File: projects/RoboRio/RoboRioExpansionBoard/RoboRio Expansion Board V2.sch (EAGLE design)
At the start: 89 parts, among them J1 RRINTERFACE-FEMALE, J2 MICROSD, Q1 5.0 MHz, T1 NPN-SOT416, U1 P8X32A-Q44, U2 24LC256ST, U3 FT232RFTR232R, U4 MC1525TO, U6 RT9193-33GB, U7 RT9193-33GB

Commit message: More updates to power supply
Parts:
- added D4: SSA34-E3/61T, diode:DIODE-DO-214AC
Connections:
- new net N$24: D4.A, J1.P1-5V, U$1.V+, U$10.V+, U$11.V+, U$12.V+, U$2.V+, U$5.V+, U$6.V+, U$7.V+, U$8.V+, U$9.V+
- new net N$25: U6.EN
- net +5V: now also D4.C; no longer U$1.V+, U$10.V+, U$11.V+, U$12.V+, U$2.V+, U$5.V+, U$6.V+, U$7.V+, U$8.V+, U$9.V+, U6.EN
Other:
- note added: "Invert then connect to CBUS 2"
- moved on the sheet: C10, C11, C12, C13, U6

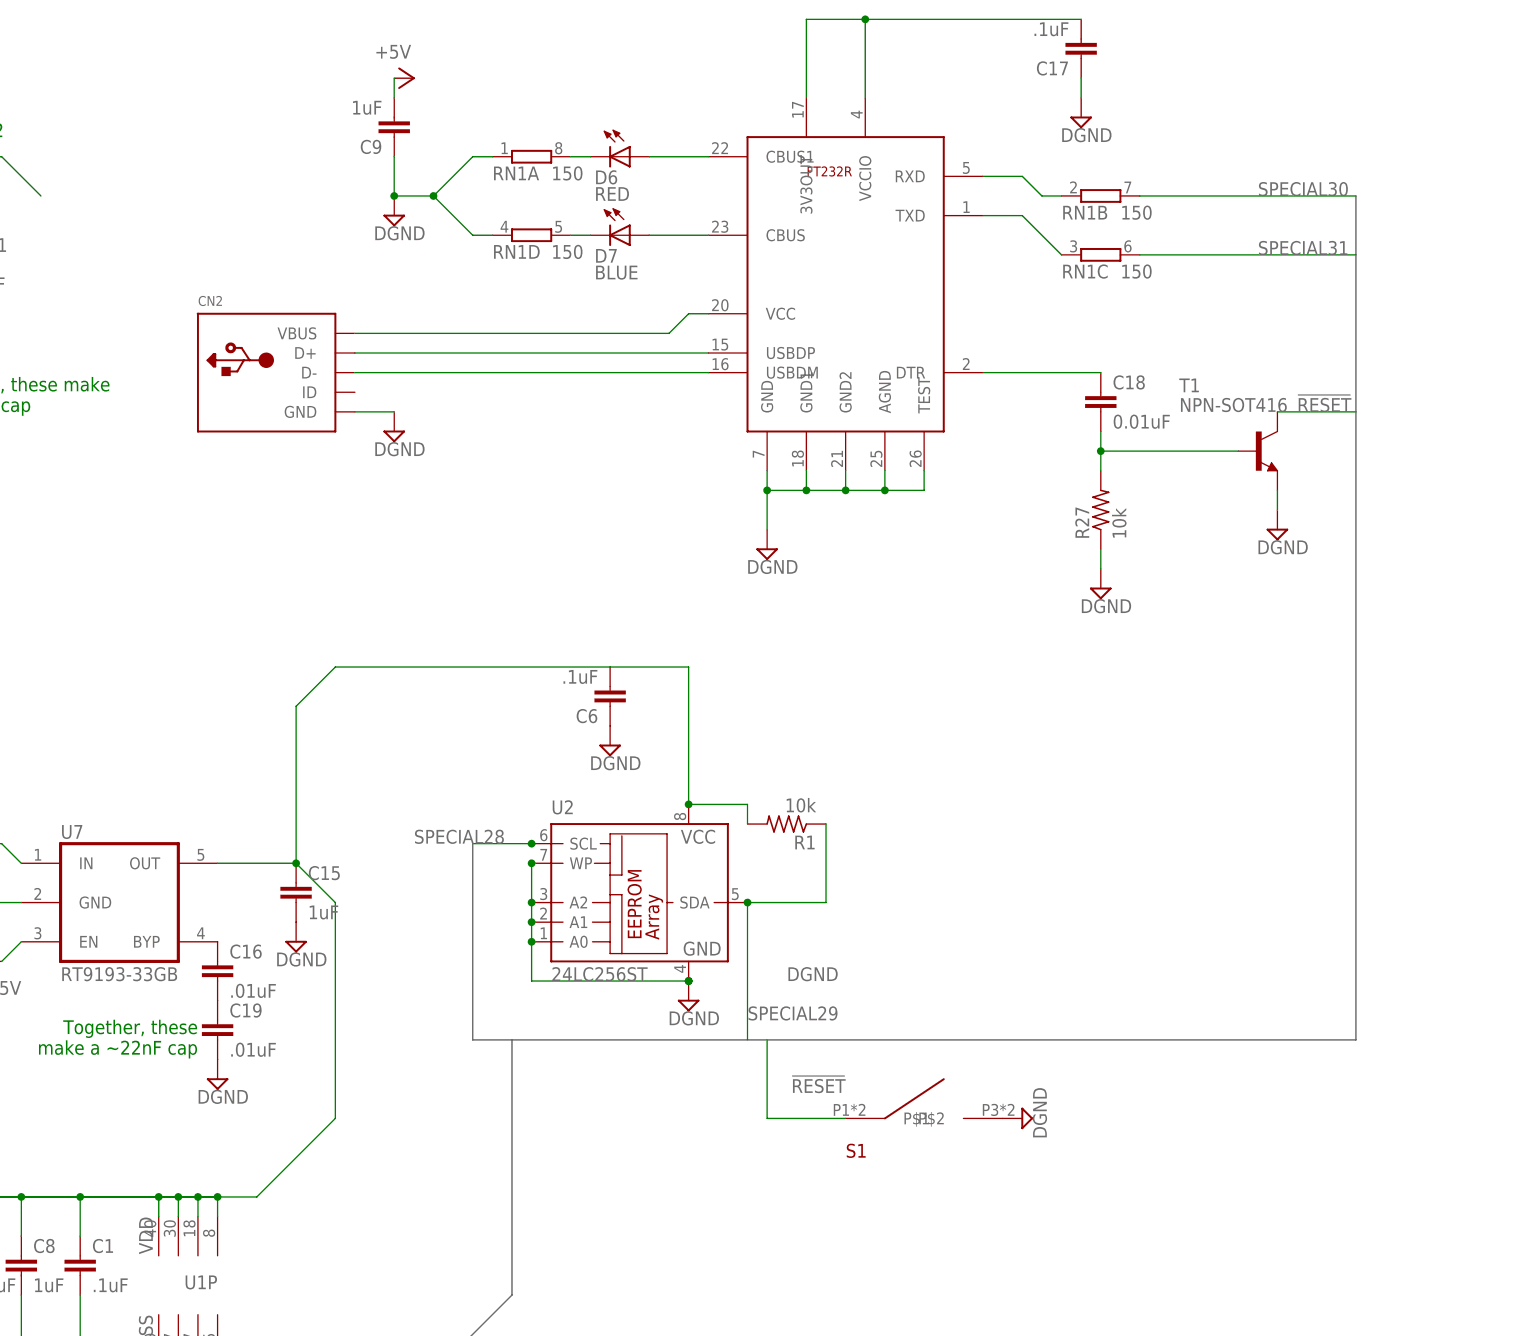
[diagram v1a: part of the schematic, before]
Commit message: Realized that we already had a full FT232R library
Switched over, prepped for the 3v3 reg, though that still needs some
help.
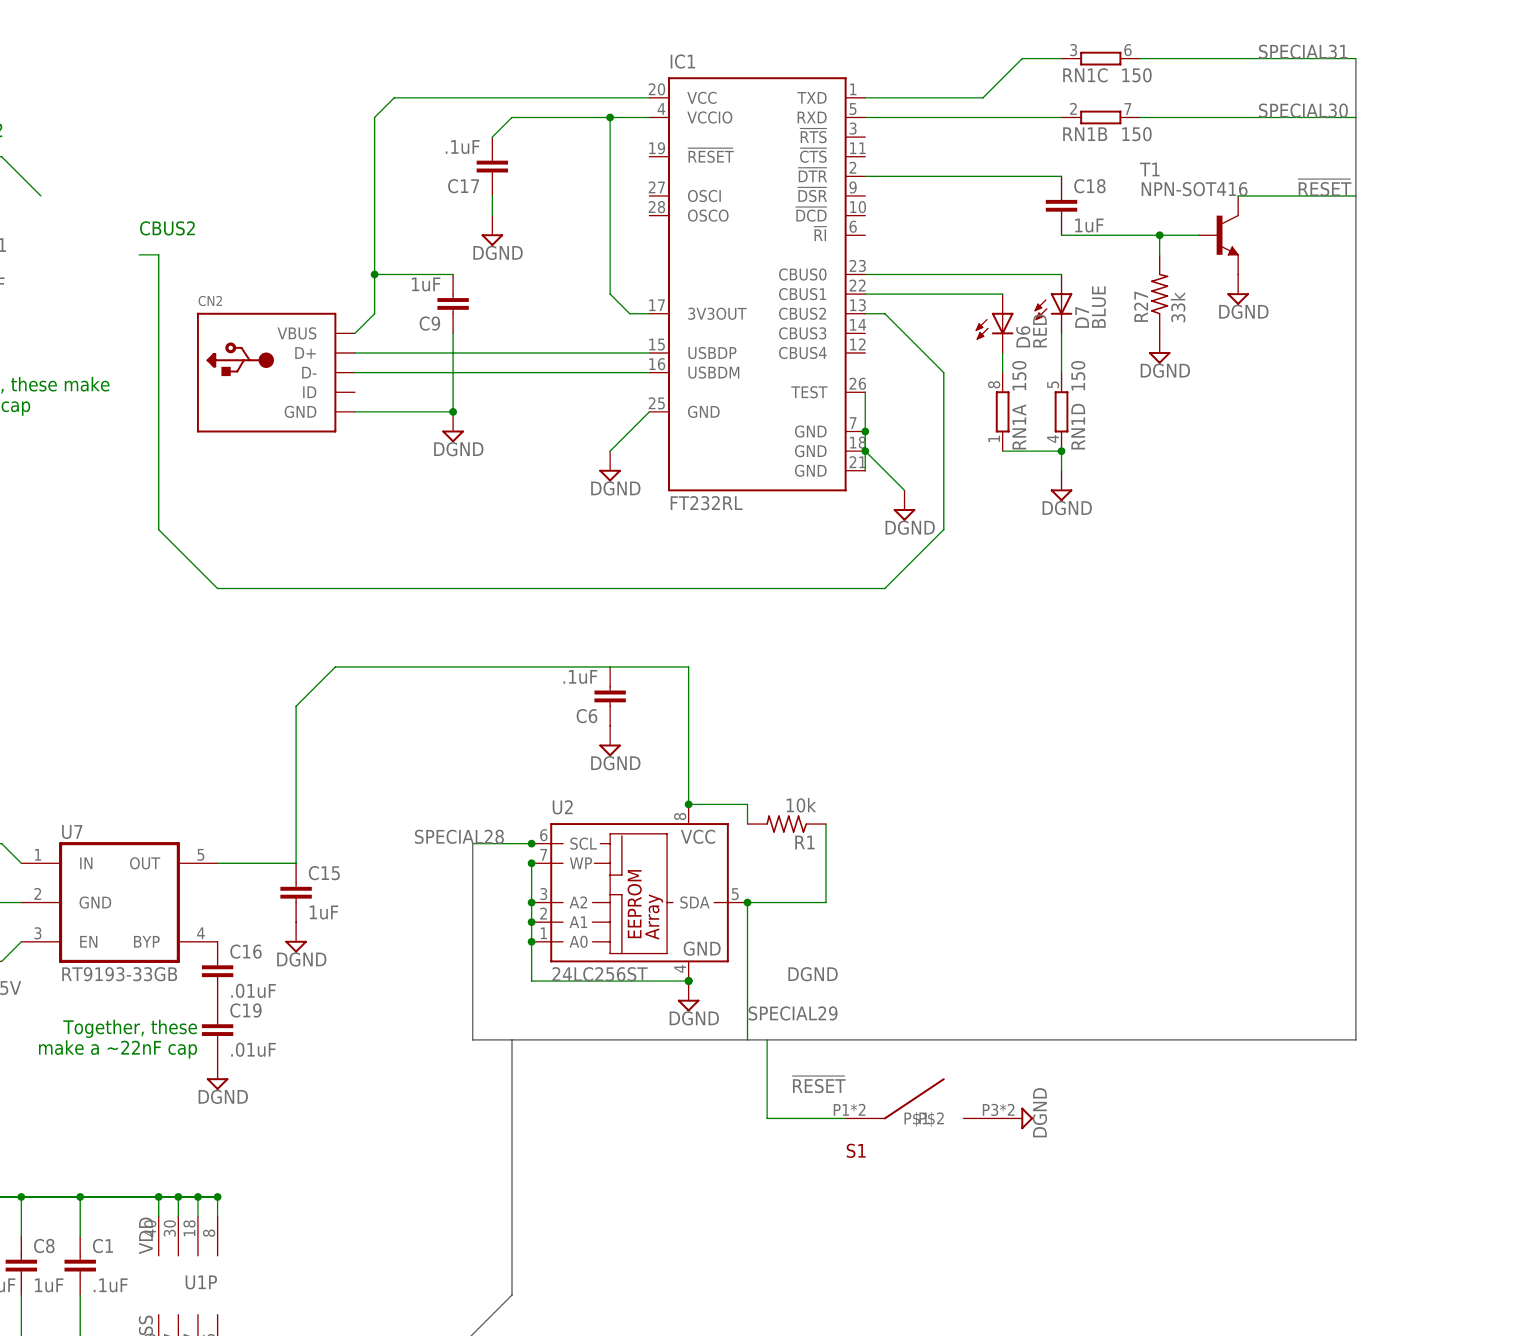
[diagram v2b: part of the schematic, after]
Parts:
- removed U3: FT232RFTR232R, FT232R:FT232RFTR232R
- added IC1: FT232RL, ftdichip:FT232RL
- C18: value 0.01uF -> 1uF
- R27: value 10k -> 33k
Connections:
- removed net N$RX: D6.A, U3.CBUS1
- removed net N$TX: D7.A, U3.CBUS
- new net N$21: C1.1, C7.1, C8.1, U1P.VDD@1, U1P.VDD@2, U1P.VDD@3, U1P.VDD@4
- new net N$27: D7.A, IC1.CBUS0
- new net N$28: D6.A, IC1.CBUS1
- new net N$31: IC1.CBUS2
- net +3V3_PROP: no longer C1.1, C7.1, C8.1, U1P.VDD@1, U1P.VDD@2, U1P.VDD@3, U1P.VDD@4
- net +5V: no longer C9.2
- net DGND: now also IC1.GND, IC1.GND@1, IC1.GND@2, IC1.GND@A, IC1.TEST; no longer U3.AGND, U3.GND, U3.GND1, U3.GND2, U3.TEST
- net N$1: now also IC1.USBDP; no longer U3.USBDP
- net N$19: now also IC1.!DTR; no longer U3.DTR
- net N$2: now also IC1.USBDM; no longer U3.USBDM
- net N$23: now also IC1.TXD; no longer U3.TXD
- net N$3: now also IC1.3V3OUT, IC1.VCCIO; no longer U3.3V3OUT, U3.VCCIO
- net N$5: now also C9.2, IC1.VCC; no longer U3.VCC
- net N$6: now also IC1.RXD; no longer U3.RXD
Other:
- note added: "CBUS2"
- moved on the sheet: C17, C18, C9, D6, D7, R27, RN1A, RN1B, RN1C, RN1D, T1

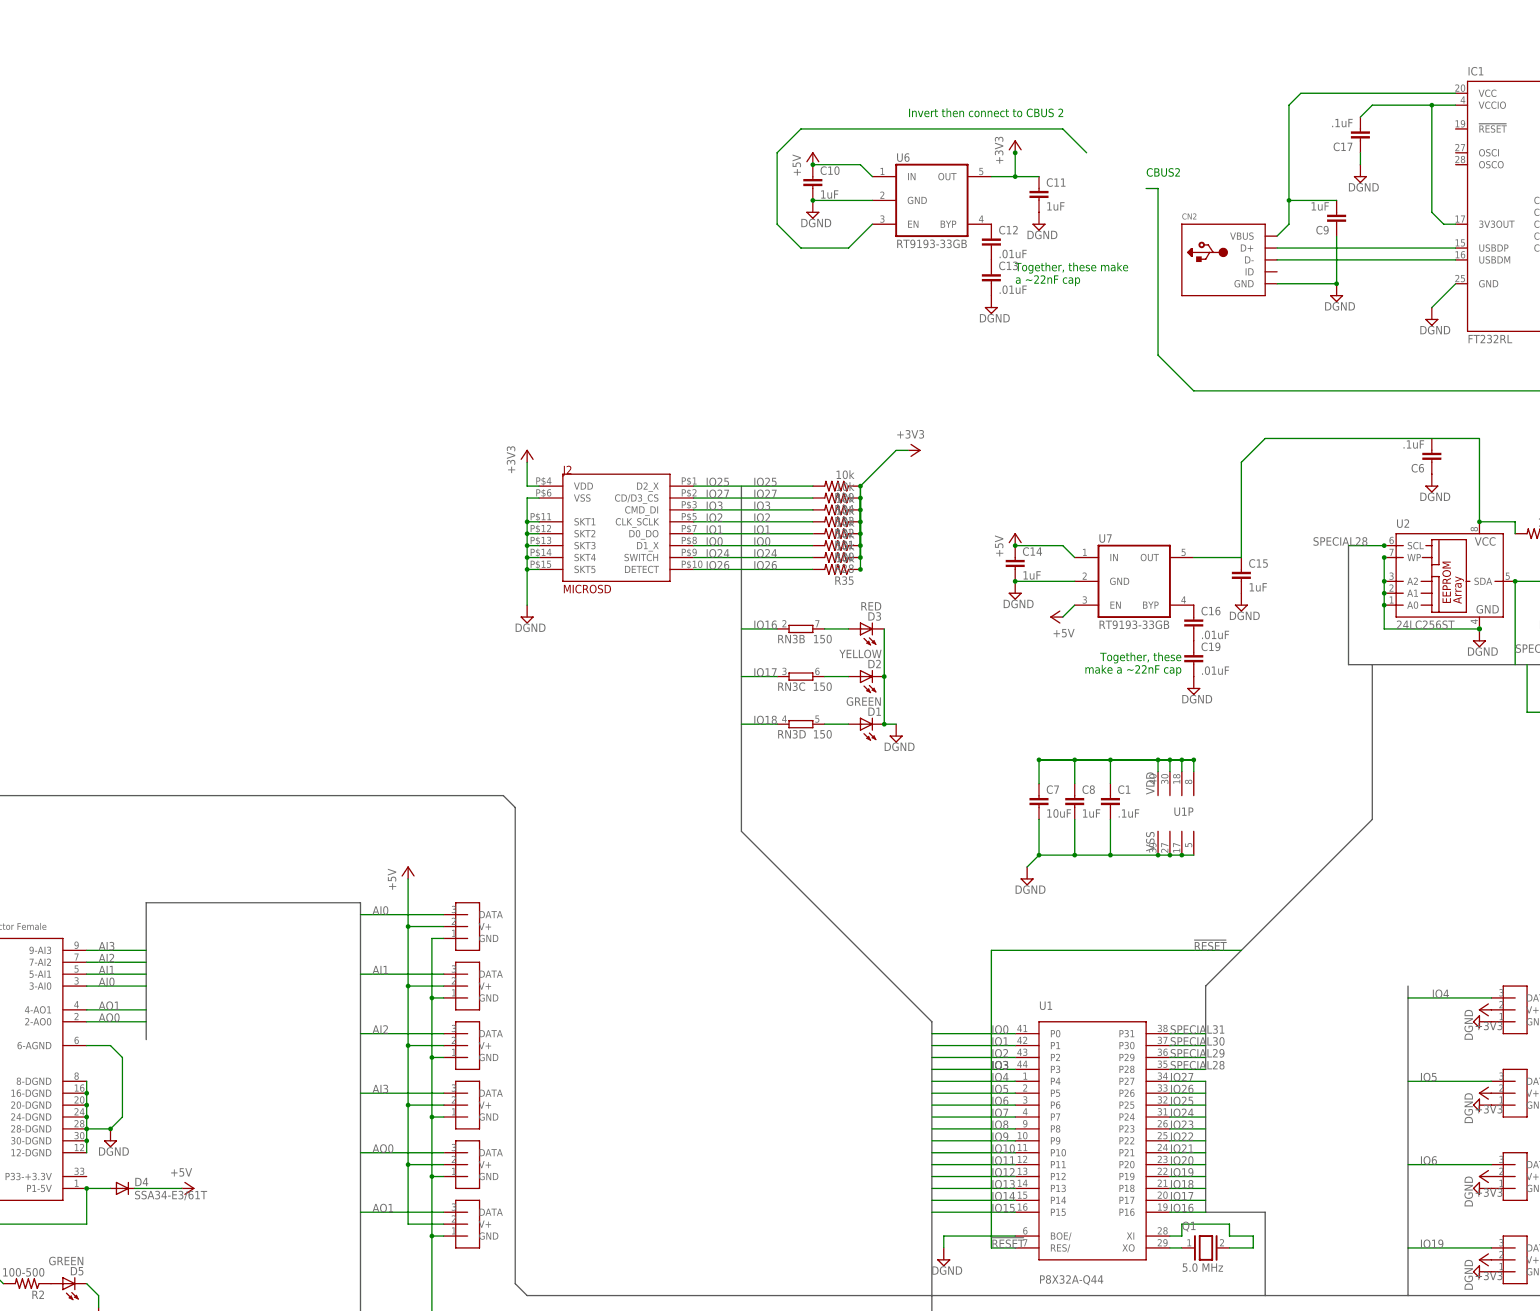
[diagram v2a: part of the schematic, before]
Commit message: all but enable inversion is ready for power supply
Need to find the part for this
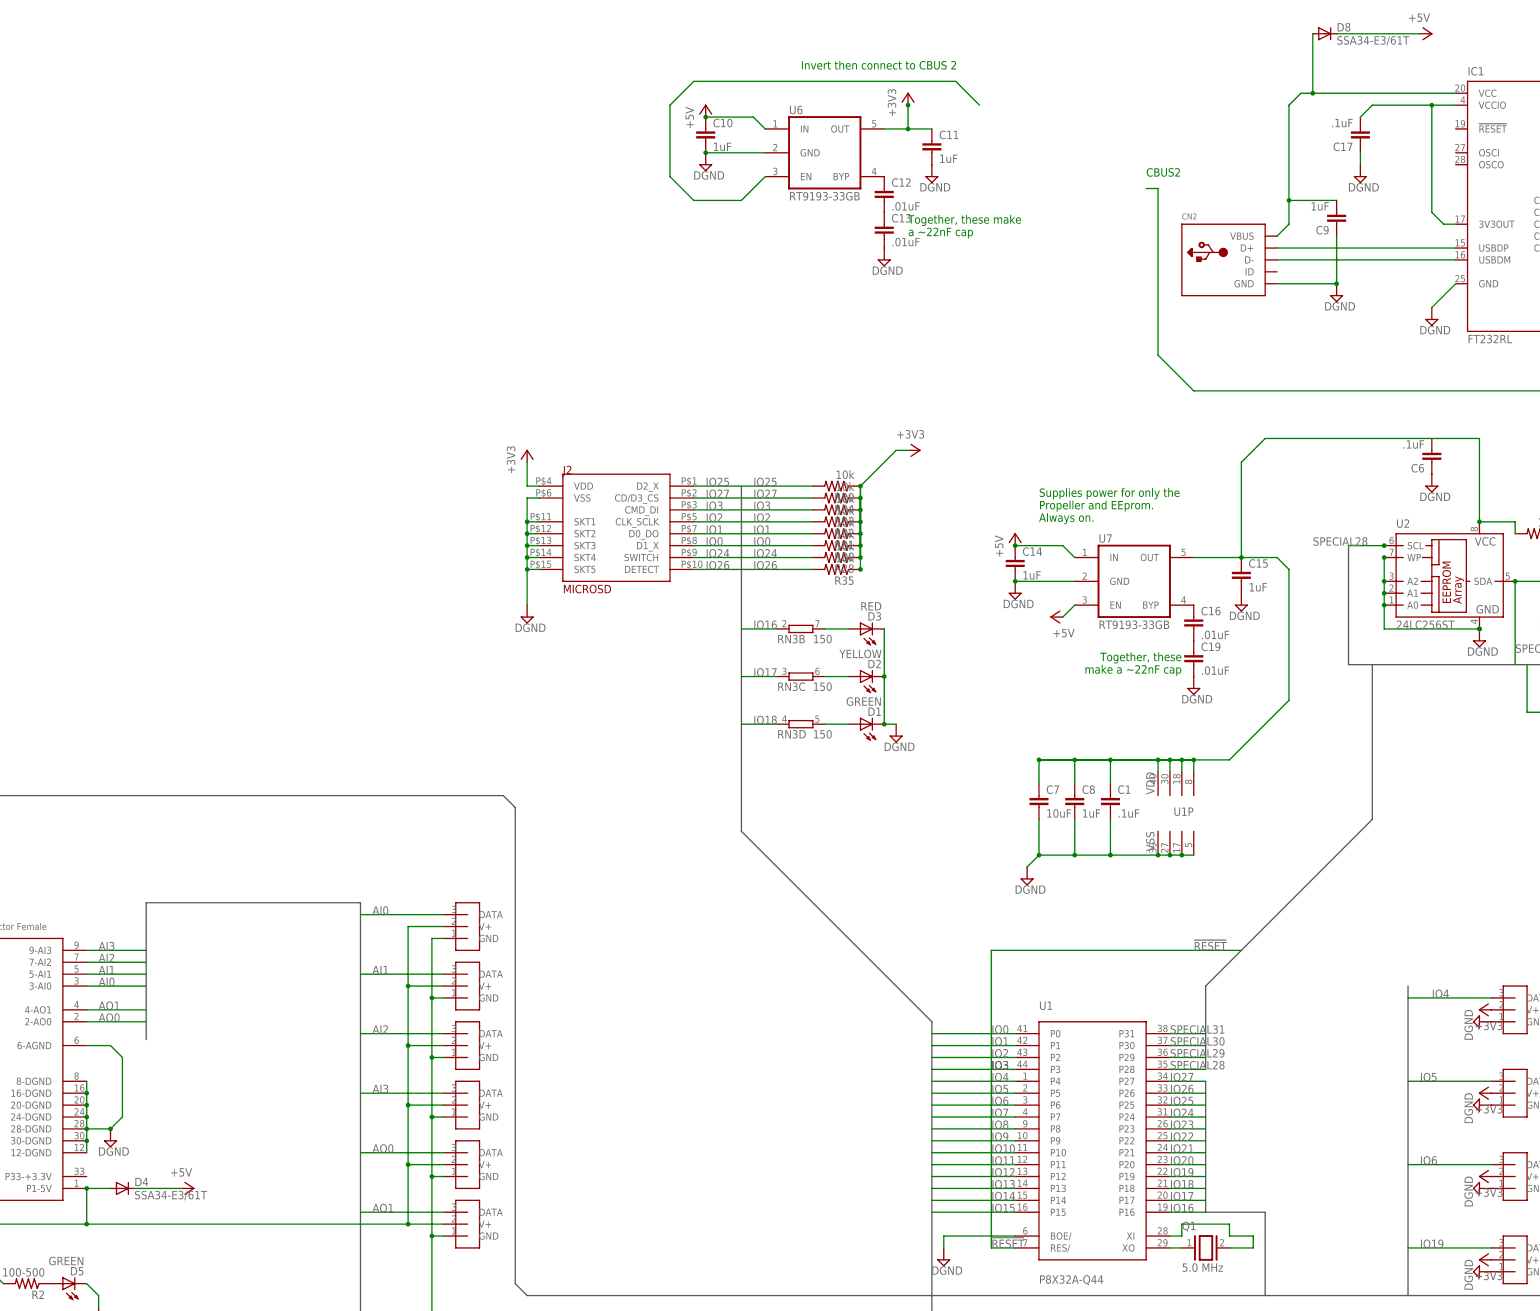
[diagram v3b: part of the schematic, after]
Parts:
- added D8: SSA34-E3/61T, diode:DIODE-DO-214AC
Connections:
- net N$31 renamed CBUS2
- removed net N$21: C1.1, C7.1, C8.1, U1P.VDD@1, U1P.VDD@2, U1P.VDD@3, U1P.VDD@4
- removed net N$24: D4.A, J1.P1-5V, U$1.V+, U$10.V+, U$11.V+, U$12.V+, U$2.V+, U$5.V+, U$6.V+, U$7.V+, U$8.V+, U$9.V+
- removed net N$5: C9.2, CN2.VBUS, IC1.VCC
- new net 5VRR: D4.A, J1.P1-5V, U$1.V+, U$10.V+, U$11.V+, U$12.V+, U$13.V+, U$14.V+, U$15.V+, U$16.V+, U$2.V+, U$3.V+, U$4.V+, U$5.V+, U$6.V+, U$7.V+, U$8.V+, U$9.V+
- new net 5VUSB: C9.2, CN2.VBUS, D8.A, IC1.VCC
- net +3V3_PROP: now also C1.1, C7.1, C8.1, U1P.VDD@1, U1P.VDD@2, U1P.VDD@3, U1P.VDD@4
- net +5V: now also D8.C; no longer U$13.V+, U$14.V+, U$15.V+, U$16.V+, U$3.V+, U$4.V+
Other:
- note added: "Supplies power for only the Propeller and EEprom. Always on."
- moved on the sheet: C10, C11, C12, C13, U6

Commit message: Added transistor for U6
As it is, it WILL NOT WORK
I am going through stuff on physical paper, and will update here when I
can.
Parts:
- added R3: 10k, resistor:R-US_R0603
- added R4: 100k - would something smaller be enought?, resistor:R-US_R0603
- added T2: NPN-SOT416, NPN transistor:NPN-SOT416
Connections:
- net 5VUSB: now also R3.2
- net CBUS2: now also R3.1, T2.B
- net DGND: now also R4.1, T2.E
- net N$25: now also R4.2, T2.C
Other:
- note removed: "CBUS2"
- note removed: "Invert then connect to CBUS 2"
- moved on the sheet: D5, D8, R1, R2
